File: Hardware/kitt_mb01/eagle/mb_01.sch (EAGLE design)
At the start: 123 parts, among them IC2.0 BQ24266RGET, IC3.01 LSM9DS1, U1.01 RT8293A, U1.02 MIC5205-3.3YM5TR, U6.01 TPS61032RSARPSDO-G16, U7.01 SI1922EDH, U7.03 SI1922EDH, U7.2 SI1922EDH, X2.01 S2B-PH-K-S(LF)(SN), X7.02 ARDUINO_UNO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

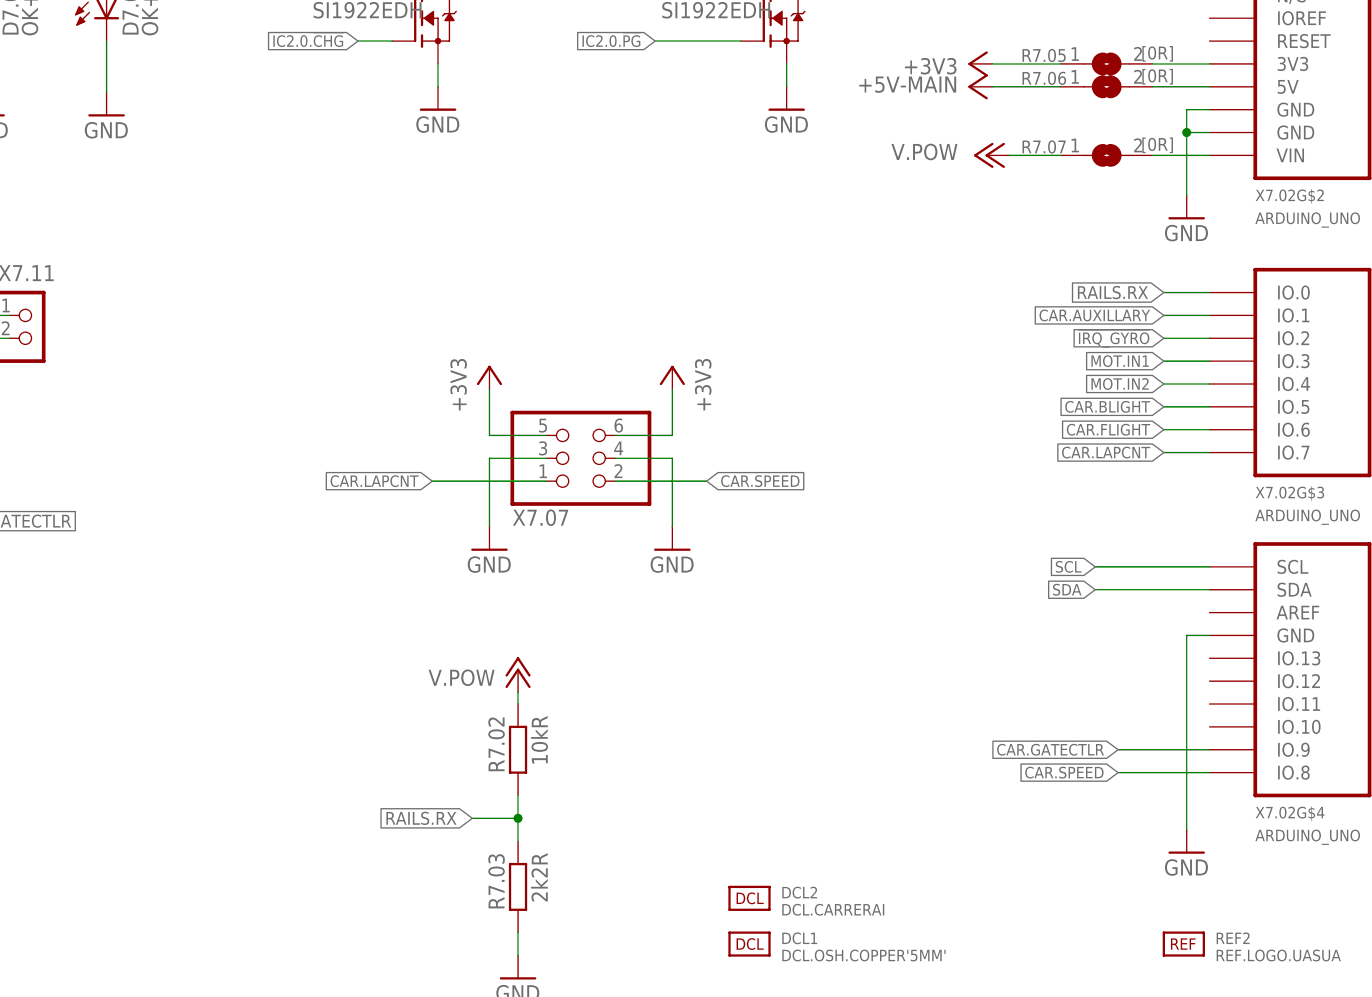
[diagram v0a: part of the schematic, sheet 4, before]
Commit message: -> added missing i2c routes -> rearranged inductor for battery charger to be in lesser proximity to the gyro
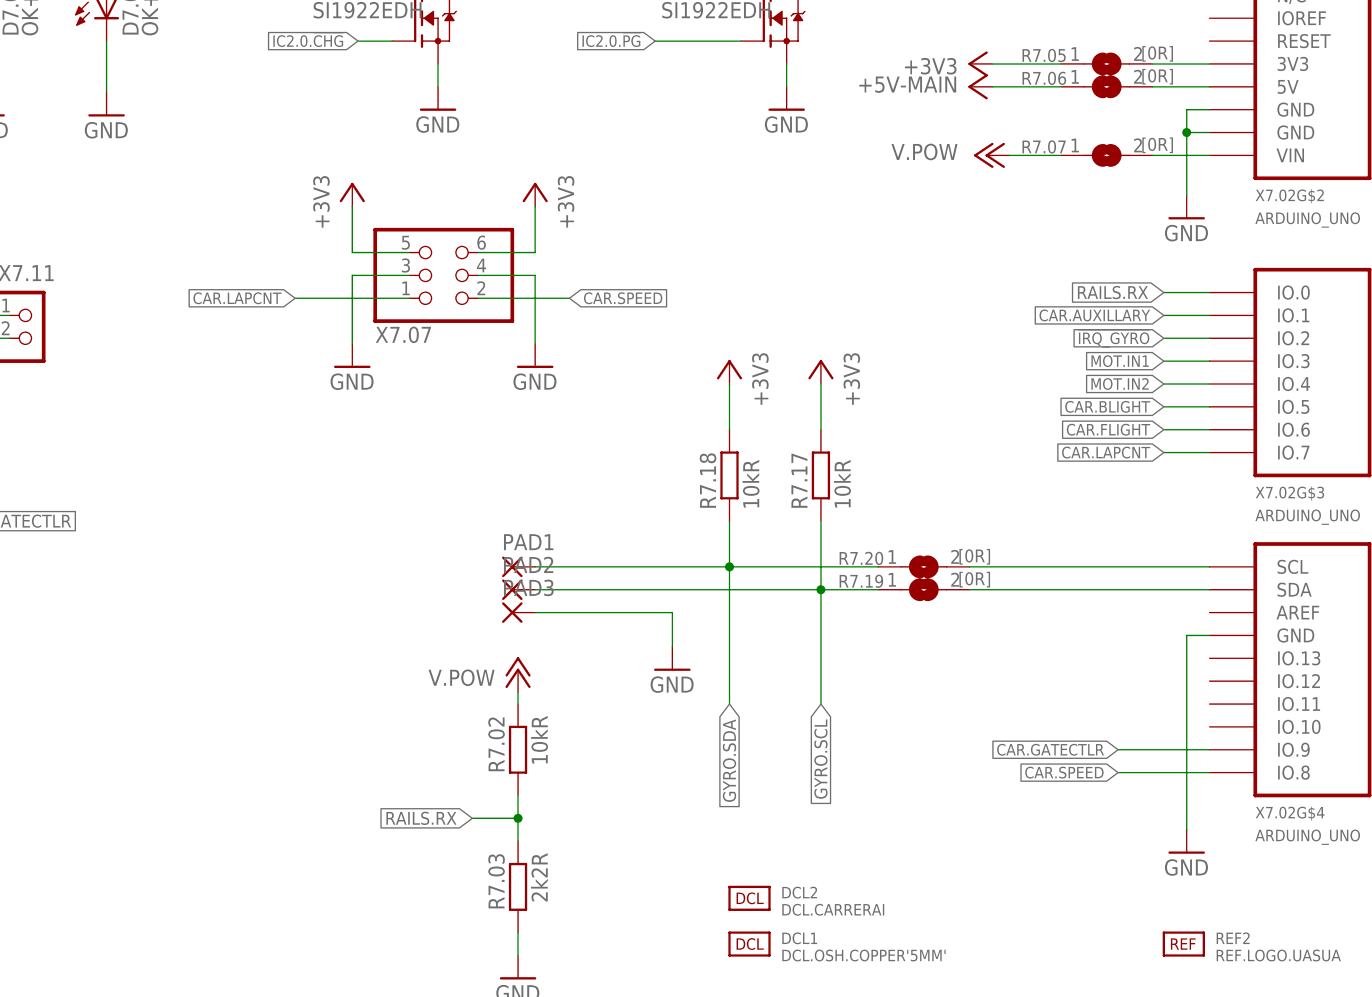
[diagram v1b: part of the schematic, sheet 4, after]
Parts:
- removed C1.07, C1.08: 1uF, rcl:CPOL-EUA/3216-18R
- removed R1.07: [0R], rcl:R-EU_R0402
- removed U1.02: MIC5205-3.3YM5TR, kitt.ic:MIC5205-3.3YM5TR
- added PAD1, PAD2, PAD3: (no value), wirepad:SMD2
- added R7.17, R7.18: 10kR, rcl:R-EU_R0402
- added R7.19, R7.20: [0R], jumper:SJ
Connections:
- removed net ARDUINO.SCL: IC3.01.SCL/SPC
- removed net ARDUINO.SDA: IC3.01.SDA/SDI/SDO
- removed net SCL: X7.02G$4.SCL
- removed net SDA: X7.02G$4.SDA
- new net GYRO.SCL: IC3.01.SCL/SPC, PAD2.P, R7.17.1, R7.19.1
- new net GYRO.SDA: IC3.01.SDA/SDI/SDO, PAD1.P, R7.18.1, R7.20.1
- new net N$53: R7.20.2, X7.02G$4.SCL
- net +3V3: now also R7.17.2, R7.18.2; no longer C1.08.+, U1.02.OUT
- net +5V: no longer C1.07.+, R1.07.2, U1.02.IN
- net GND: now also PAD3.P; no longer C1.07.-, C1.08.-, U1.02.GND
- net N$49: now also R7.19.2, X7.02G$4.SDA; no longer R1.07.1, U1.02.EN
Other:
- note added: "FIX VDRV????"
- note added: "TODO TP"
- note added: "WHERE DOES IT LEAD WHERE DOES IT GO DIDDY DAE YAY COTTON EYE JOE"
- note removed: "TODO"
- moved on the sheet: X7.07

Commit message: redid some routes, they seem more optimized
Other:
- note removed: "WHERE DOES IT LEAD WHERE DOES IT GO DIDDY DAE YAY COTTON EYE JOE"
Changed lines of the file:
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@@
 Trainable Trackcars</text>
 <text x="162.56" y="16.51" size="2.1844" layer="94">MotorBoard 01</text>
-<text x="-10.16" y="96.52" size="1.778" layer="98">WHERE DOES IT LEAD WHERE DOES IT GO
-DIDDY DAE YAY COTTON EYE JOE</text>
-<text x="22.86" y="91.44" size="1.778" layer="98">FIX VDRV????</text>
+<text x="10.16" y="91.44" size="1.778" layer="98">FIX VDRV????</text>
 </plain>
 <instances>

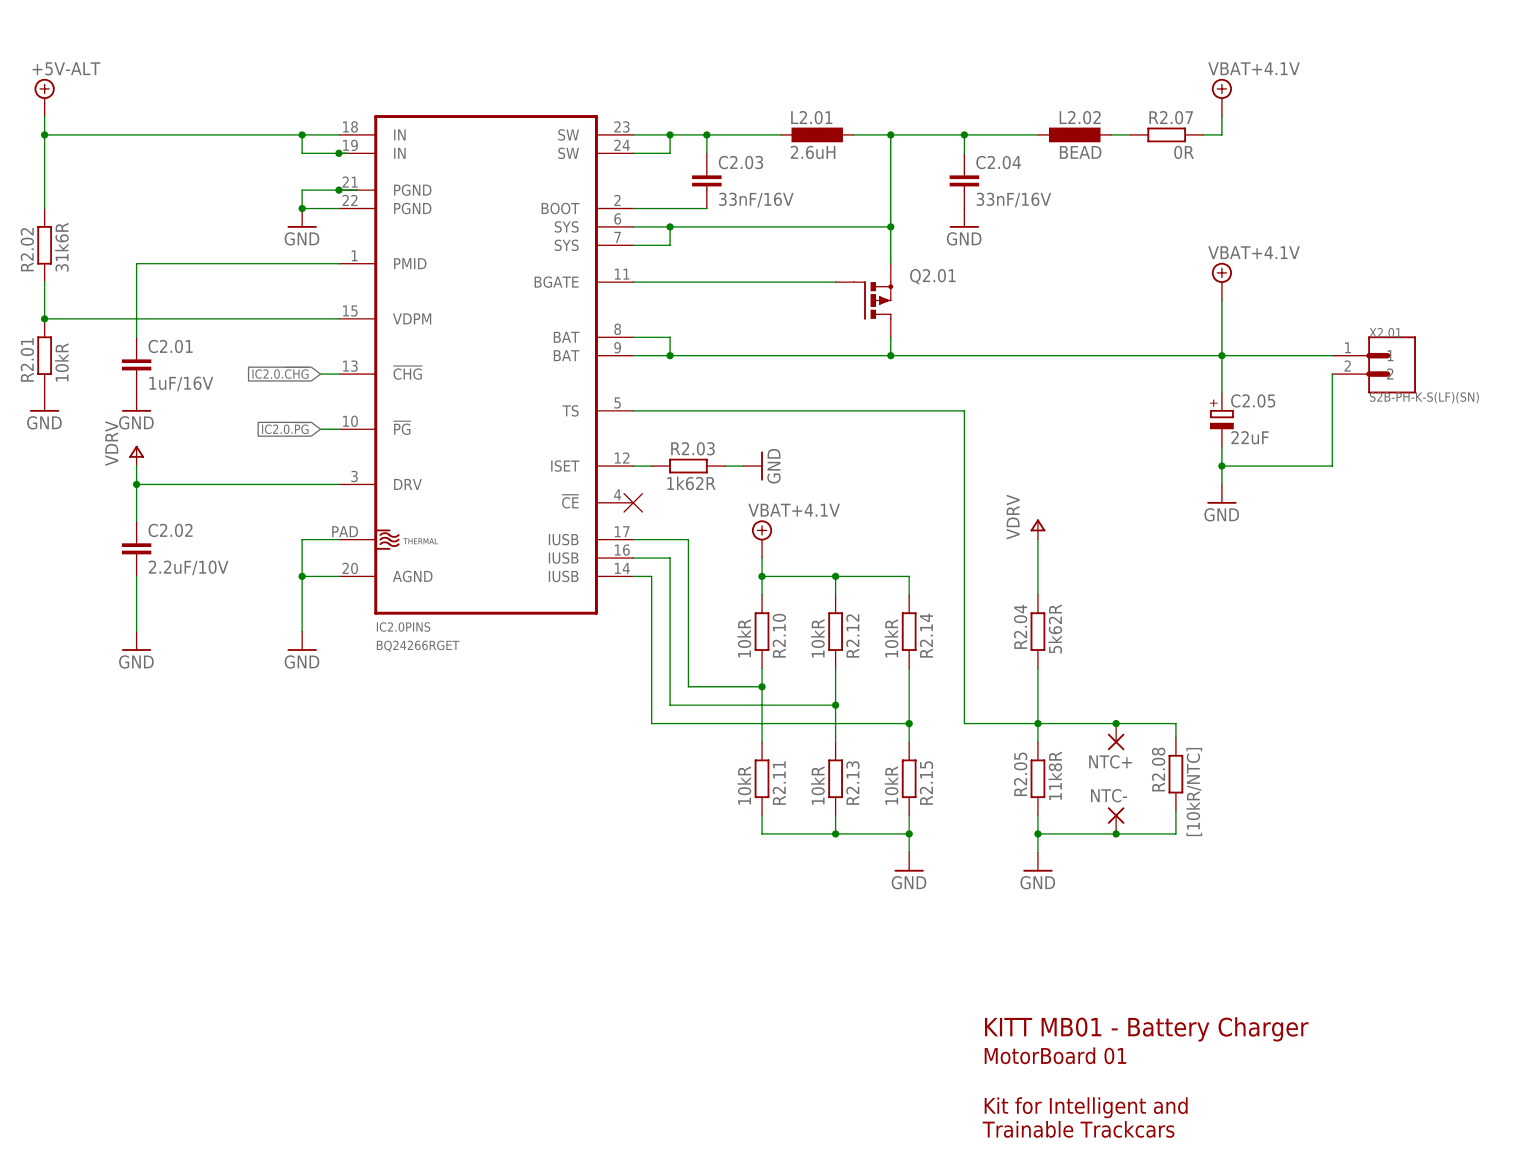
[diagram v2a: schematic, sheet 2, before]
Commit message: even more optimizations happened in subgroup 2XX -> less vias -> caps closer to IC -> added "hacking" resistor R213 to enable bodge-jobbing !CE
todo:
-> remove dots between identifiers to save precious silk screen real estate
-> run the DRC, plus ERC
-> scale down and re-place logo
-> more testpoints, it's low-effort for a potential high-payout when murphy strikes again
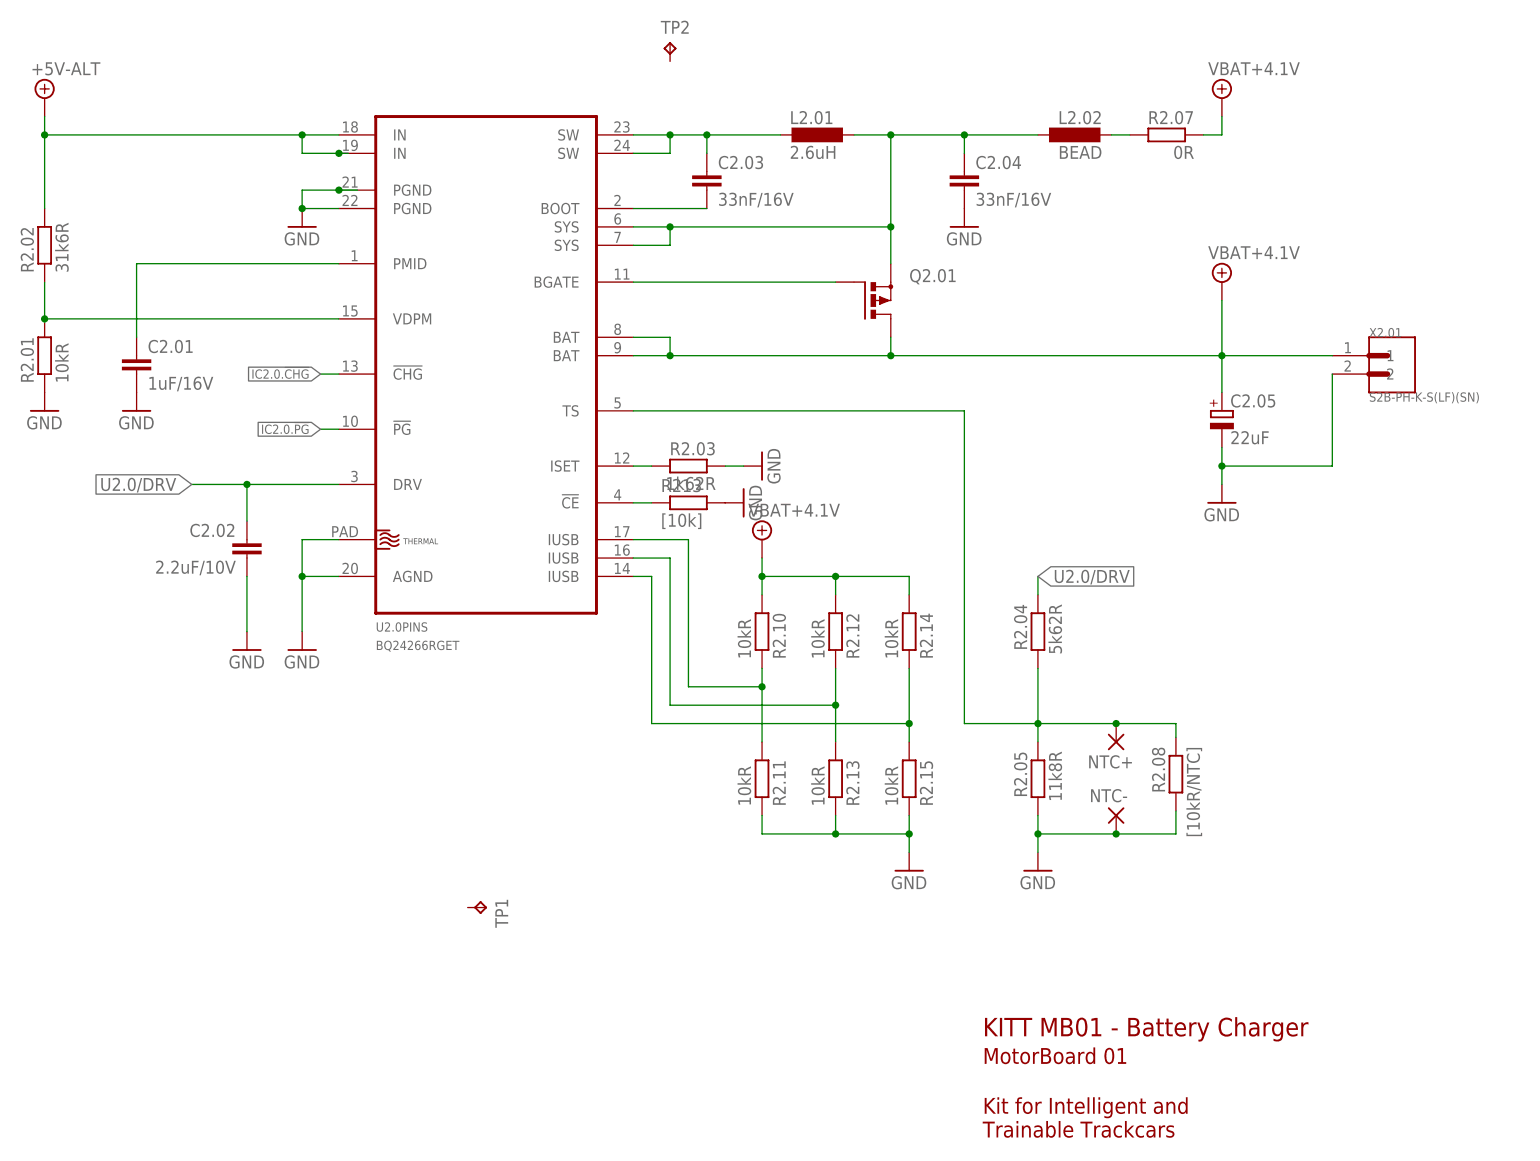
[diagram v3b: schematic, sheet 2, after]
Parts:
- added R213: [10k], rcl:R-EU_01005
- added TP1, TP2: TPTP07R, testpad:TPTP07R
- renumbered IC2.0 to U2.0
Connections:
- net N$12 renamed U2.0/SW
- net N$13 renamed U2.0/BOOT
- net N$14 renamed U2.0/BGATE
- net N$15 renamed U2.0/TS
- net N$18 renamed U2.0/SYS
- net N$8 renamed U2.0/PMID
- net V+ renamed U2.0/DRV
- new net N$8: R213.1, U2.0PINS.!CE
- net GND: now also R213.2
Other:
- note removed: "FIX VDRV????"
- moved on the sheet: C2.02
